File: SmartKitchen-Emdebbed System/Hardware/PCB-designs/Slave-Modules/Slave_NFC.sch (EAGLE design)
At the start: 34 parts, among them IC1 PCF8574T, IC2 7805DT, IC3 PCF8574T, IC4 74AHC1G126DBV, J1 RJ11-2L-B, J2 RJ11-2L-B, Q1 SPB80P06P, Q2 SPB80P06P, Q3 SPB80P06P, X1 22-23-2101

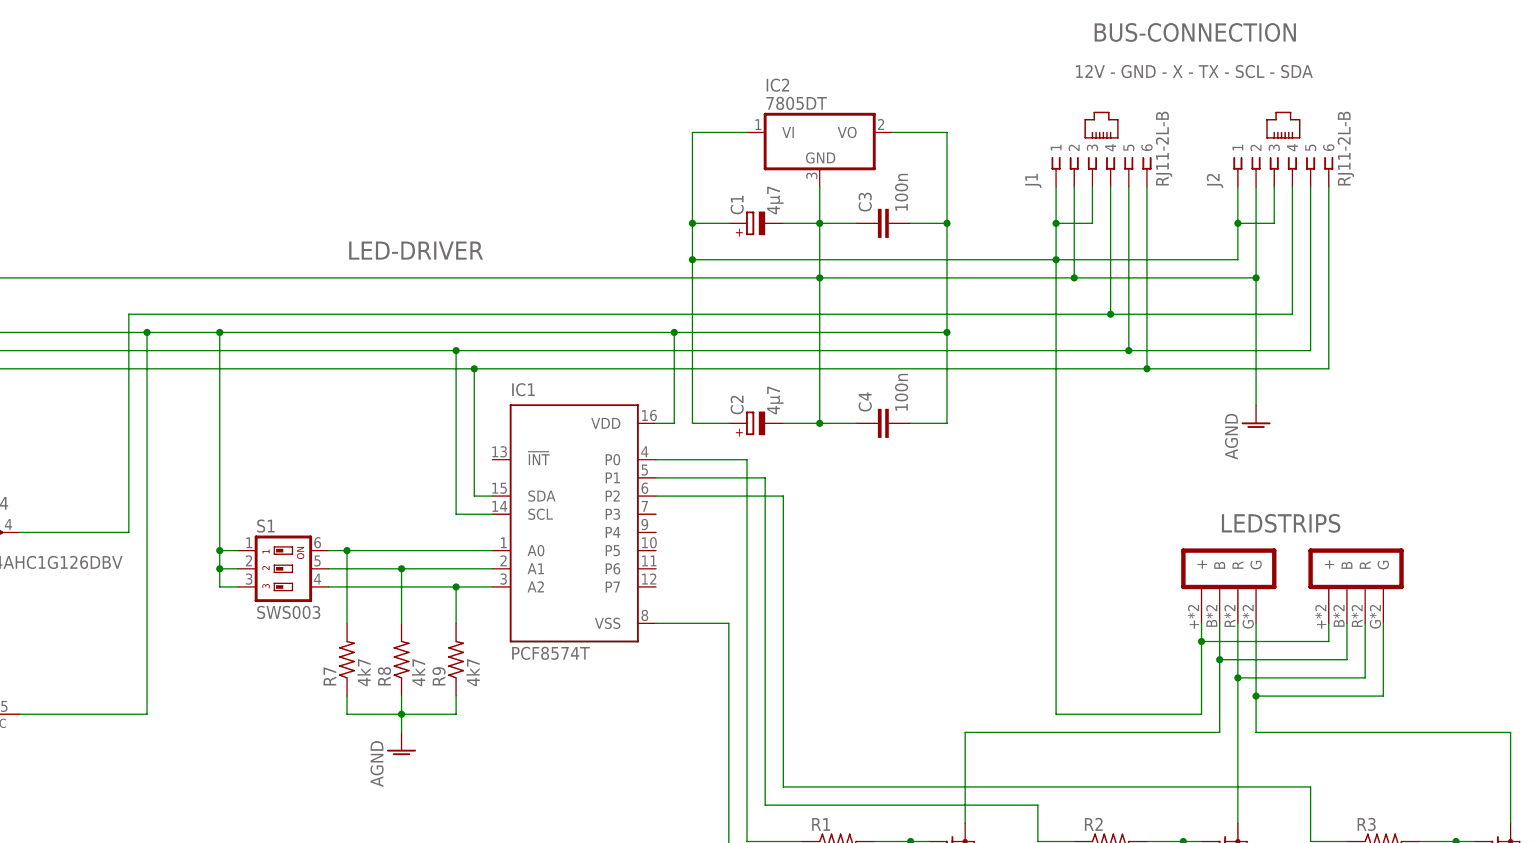
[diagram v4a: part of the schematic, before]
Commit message: adding pull-ups and inh-capacitors to list
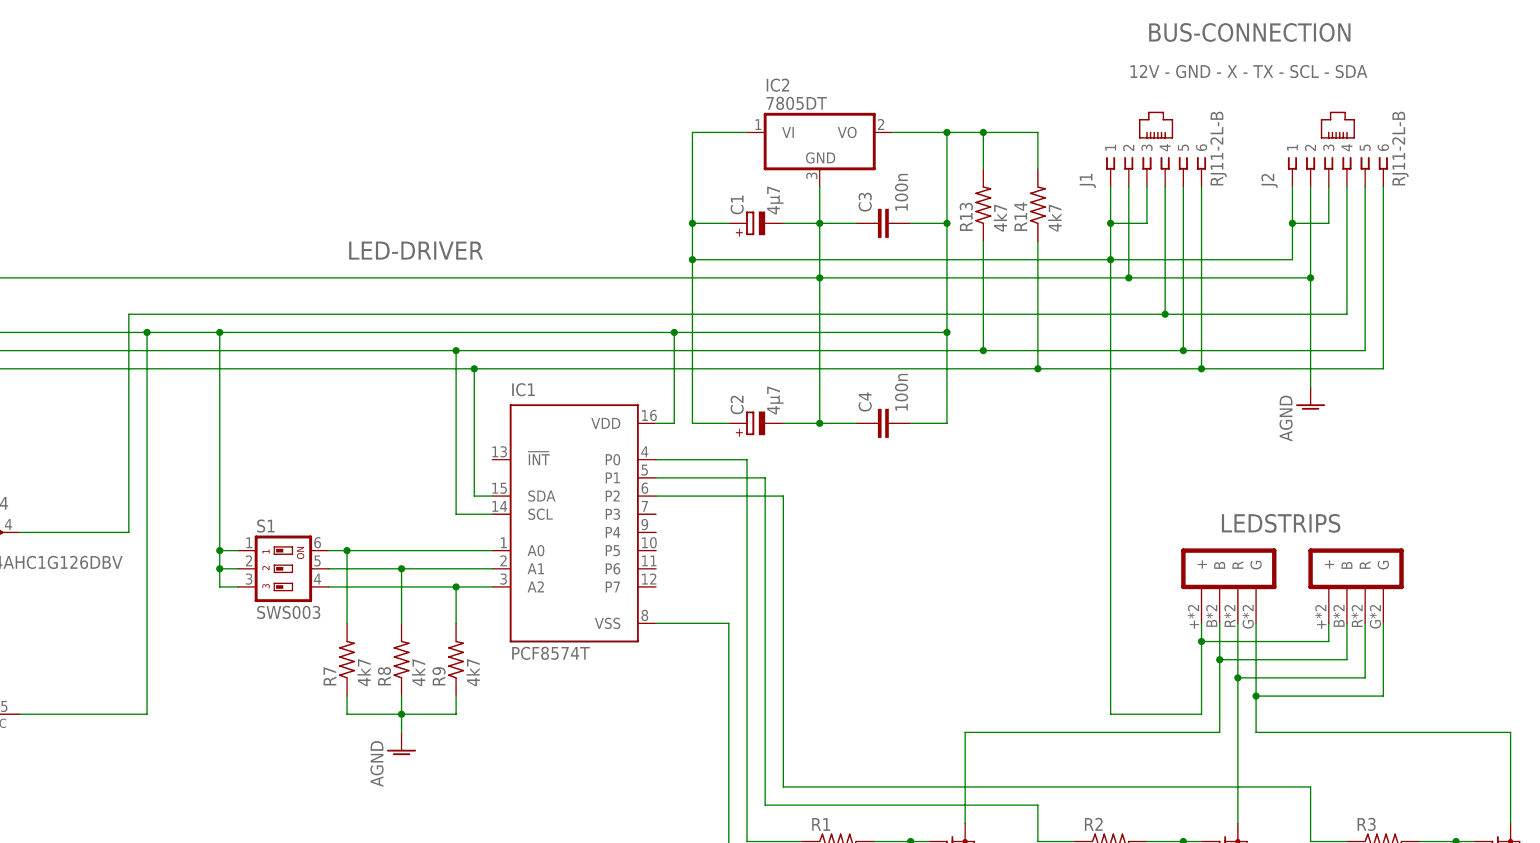
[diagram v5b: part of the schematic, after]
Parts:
- added R13, R14: 4k7, rcl:R-US_R0402
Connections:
- net N$1: now also R14.1
- net N$21: now also R13.2, R14.2
- net N$3: now also R13.1
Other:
- moved on the sheet: J1, J2

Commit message: Adding planes and references
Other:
- note added: "POWER REGULATOR"
- note added: "SMART FRIDGE PROJECT"
- note added: "Tom Mampaey"
- moved on the sheet: C1, C2, C3, C4, IC1, IC2, IC3, IC4, IC4P, INDILED, J1, J2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
